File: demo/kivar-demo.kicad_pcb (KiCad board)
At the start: 2 copper layers, 59 x 42 mm, 66 parts, among them U1 24C02, U2 MIC841HYC5, U3 ISL91127IRAZ, U4 TCA9535PWR, U6 AP3032, U7 LDO

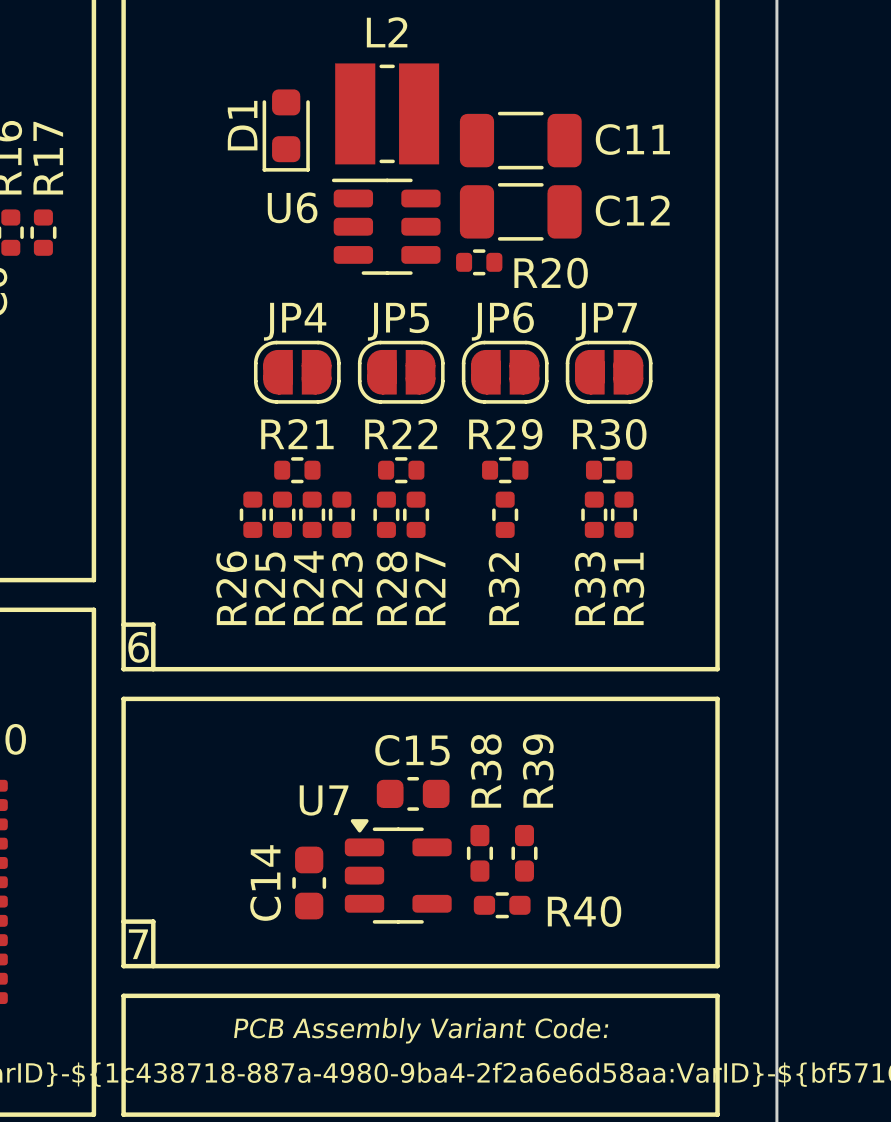
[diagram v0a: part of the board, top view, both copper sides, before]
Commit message: Fix demo project for 0.4.0 re-release
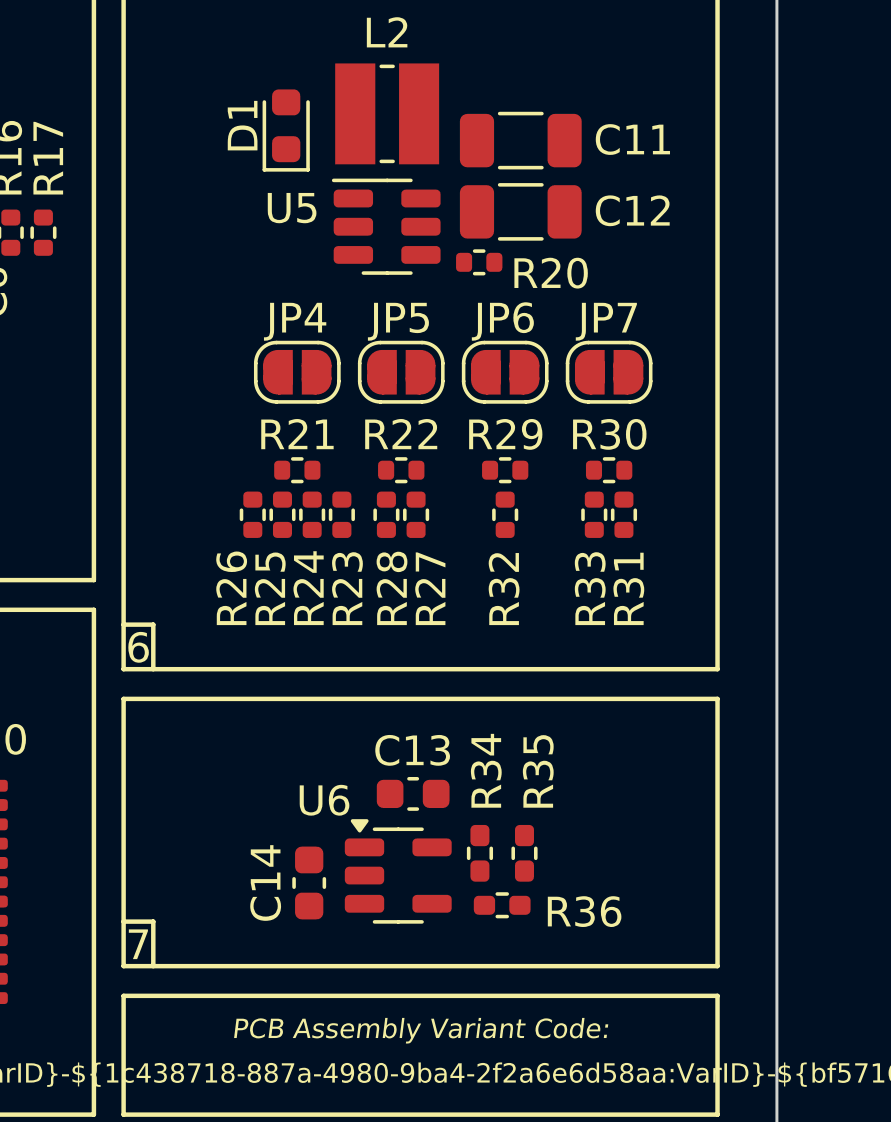
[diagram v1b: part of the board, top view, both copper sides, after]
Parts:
- renumbered C15 to C13, R38 to R34, R39 to R35, R40 to R36, U6 to U5, U7 to U6
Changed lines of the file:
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@@
 	(title_block
 		(title "KiVar Demo Board")
-		(date "2024-09-14")
+		(date "2024-09-16")
 		(rev "0.4.0")
 		(company "Author: Mark Hämmerling <dev@markh.de>")
@@
 	(net 55 "+5V")
 	(net 56 "/Example 7: LDO Output Voltage Selection/VOUT")
-	(net 57 "Net-(U7-FB)")
+	(net 57 "Net-(U6-FB)")
 	(footprint "Resistor_SMD:R_0402_1005Metric"
 		(layer "F.Cu")
@@
 			(at 0 1.17 90)
 			(layer "F.Fab")
+			(hide yes)
 			(effects
 				(font
@@
 			(at 0 1.17 0)
 			(layer "F.Fab")
+			(hide yes)
 			(effects
 				(font
@@
 			(at 0 1.17 90)
 			(layer "F.Fab")
+			(hide yes)
 			(effects
 				(font
@@
 		(descr "SOT, 5 Pin (https://www.jedec.org/sites/default/files/docs/Mo-178c.PDF variant AA), generated with kicad-footprint-generator ipc_gullwing_generator.py")
 		(tags "SOT TO_SOT_SMD")
-		(property "Reference" "U7"
+		(property "Reference" "U6"
 			(at -2.5 -2.5 0)
 			(layer "F.SilkS")
@@
 			(at 0 2.4 0)
 			(layer "F.Fab")
+			(hide yes)
 			(effects
 				(font
@@
 			(layers "F.Cu" "F.Paste" "F.Mask")
 			(roundrect_rratio 0.25)
-			(net 57 "Net-(U7-FB)")
+			(net 57 "Net-(U6-FB)")
 			(pinfunction "FB")
 			(pintype "input")
@@
 			(at 0 1.9 0)
 			(layer "F.Fab")
+			(hide yes)
 			(effects
 				(font
@@
 		(descr "Resistor SMD 0402 (1005 Metric), square (rectangular) end terminal, IPC_7351 nominal with elongated pad for handsoldering. (Body size source: IPC-SM-782 page 72, https://www.pcb-3d.com/wordpress/wp-content/uploads/ipc-sm-782a_amendment_1_and_2.pdf), generated with kicad-footprint-generator")
 		(tags "resistor handsolder")
-		(property "Reference" "R40"
+		(property "Reference" "R36"
 			(at -2.75 -0.25 0)
 			(layer "F.SilkS")
@@
 			(at 0 1.17 0)
 			(layer "F.Fab")
+			(hide yes)
 			(effects
 				(font
@@
 			(layers "F.Cu" "F.Paste" "F.Mask")
 			(roundrect_rratio 0.25)
-			(net 57 "Net-(U7-FB)")
+			(net 57 "Net-(U6-FB)")
 			(pintype "passive")
 		)
@@
 			(at 0 1.43 90)
 			(layer "F.Fab")
+			(hide yes)
 			(effects
 				(font
@@
 			(at 0 1.17 0)
 			(layer "F.Fab")
+			(hide yes)
 			(effects
 				(font
@@
 			(at 0 1.17 90)
 			(layer "F.Fab")
+			(hide yes)
 			(effects
 				(font
@@
 			(at 0 1.85 0)
 			(layer "F.Fab")
+			(hide yes)
 			(effects
 				(font
@@
 			(at 0 1.17 0)
 			(layer "F.Fab")
+			(hide yes)
 			(effects
 				(font
@@
 			(at 0 3.2 0)
 			(layer "F.Fab")
+			(hide yes)
 			(effects
 				(font
@@
 			(at 0 1.9 0)
 			(layer "F.Fab")
+			(hide yes)
 			(effects
 				(font
@@
 		(descr "Capacitor SMD 0603 (1608 Metric), square (rectangular) end terminal, IPC_7351 nominal, (Body size source: IPC-SM-782 page 76, https://www.pcb-3d.com/wordpress/wp-content/uploads/ipc-sm-782a_amendment_1_and_2.pdf), generated with kicad-footprint-generator")
 		(tags "capacitor")
-		(property "Reference" "C15"
+		(property "Reference" "C13"
 			(at 0 -1.43 0)
 			(layer "F.SilkS")
@@
 			(at 0 1.43 0)
 			(layer "F.Fab")
+			(hide yes)
 			(effects
 				(font
@@
 			(at 0 1.17 90)
 			(layer "F.Fab")
+			(hide yes)
 			(effects
 				(font
@@
 		(descr "Resistor SMD 0402 (1005 Metric), square (rectangular) end terminal, IPC_7351 nominal with elongated pad for handsoldering. (Body size source: IPC-SM-782 page 72, https://www.pcb-3d.com/wordpress/wp-content/uploads/ipc-sm-782a_amendment_1_and_2.pdf), generated with kicad-footprint-generator")
 		(tags "resistor handsolder")
-		(property "Reference" "R38"
+		(property "Reference" "R34"
 			(at -2.75 -0.25 90)
 			(layer "F.SilkS")
@@
 			(at 0 1.17 90)
 			(layer "F.Fab")
+			(hide yes)
 			(effects
 				(font
@@
 			)
 		)
-		(property "Var" "1.2V(0Ω) 1.8V(100kΩ) 3.3V(175kΩ)"
+		(property "Var" "1.2V(0Ω) 1.8V(100kΩ) 2.5V(150kΩ) 3.3V(175kΩ)"
 			(at 0 0 -90)
 			(unlocked yes)
@@
 			)
 		)
-		(property "VarID.Var" "1.2V(12) 1.8V(18) 3.3V(33)"
+		(property "VarID.Var" "1.2V(12) 1.8V(18) 2.5V(25) 3.3V(33)"
 			(at 0 0 -90)
 			(unlocked yes)
@@
 			(layers "F.Cu" "F.Paste" "F.Mask")
 			(roundrect_rratio 0.25)
-			(net 57 "Net-(U7-FB)")
+			(net 57 "Net-(U6-FB)")
 			(pintype "passive")
 		)
@@
 			(at 0 1.17 90)
 			(layer "F.Fab")
+			(hide yes)
 			(effects
 				(font
@@
 			(at 0 1.17 0)
 			(layer "F.Fab")
+			(hide yes)
 			(effects
 				(font
@@
 			(at 0 1.85 0)
 			(layer "F.Fab")
+			(hide yes)
 			(effects
 				(font
@@
 			(at 0 1.17 0)
 			(layer "F.Fab")
+			(hide yes)
 			(effects
 				(font
@@
 			(at 0 1.9 0)
 			(layer "F.Fab")
+			(hide yes)
 			(effects
 				(font
@@
 			(at 0 1.17 90)
 			(layer "F.Fab")
+			(hide yes)
 			(effects
 				(font
@@
 			(at 0 1.17 90)
 			(layer "F.Fab")
+			(hide yes)
 			(effects
 				(font
@@
 			(at 0 1.17 90)
 			(layer "F.Fab")
+			(hide yes)
 			(effects
 				(font
@@
 			(at 0 1.17 90)
 			(layer "F.Fab")
+			(hide yes)
 			(effects
 				(font
@@
 			(at 0 1.43 -90)
 			(layer "F.Fab")
+			(hide yes)
 			(effects
 				(font
@@
 			(at 0 1.9 0)
 			(layer "F.Fab")
+			(hide yes)
 			(effects
 				(font
@@
 		(descr "SOT, 6 Pin (https://www.jedec.org/sites/default/files/docs/Mo-178c.PDF variant AB), generated with kicad-footprint-generator ipc_gullwing_generator.py")
 		(tags "SOT TO_SOT_SMD")
-		(property "Reference" "U6"
+		(property "Reference" "U5"
 			(at -3.2 -0.6 0)
 			(layer "F.SilkS")
@@
 			(at 0 2.4 0)
 			(layer "F.Fab")
+			(hide yes)
 			(effects
 				(font
@@
 		(descr "Resistor SMD 0402 (1005 Metric), square (rectangular) end terminal, IPC_7351 nominal with elongated pad for handsoldering. (Body size source: IPC-SM-782 page 72, https://www.pcb-3d.com/wordpress/wp-content/uploads/ipc-sm-782a_amendment_1_and_2.pdf), generated with kicad-footprint-generator")
 		(tags "resistor handsolder")
-		(property "Reference" "R39"
+		(property "Reference" "R35"
 			(at -2.75 -0.5 90)
 			(layer "F.SilkS")
@@
 			(at 0 1.17 90)
 			(layer "F.Fab")
+			(hide yes)
 			(effects
 				(font
@@
 			)
 		)
-		(property "Var" "1.8V(100kΩ) ?(DNP -s!)"
+		(property "Var" "1.8V(100kΩ) 2.5V(390kΩ) ?(DNP -s!)"
 			(at 0 0 -90)
 			(unlocked yes)
@@
 			(layers "F.Cu" "F.Paste" "F.Mask")
 			(roundrect_rratio 0.25)
-			(net 57 "Net-(U7-FB)")
+			(net 57 "Net-(U6-FB)")
 			(pintype "passive")
 		)

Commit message: Update doc info
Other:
- board text added: "https://kivar.markh.de"
- board text removed: "https://github.com/markh-de/KiVar"
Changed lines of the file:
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@@
 	(title_block
 		(title "KiVar Demo Board")
-		(date "2024-09-16")
-		(rev "0.4.0")
+		(date "2025-04-22")
+		(rev "0.5.0")
 		(company "Author: Mark Hämmerling <dev@markh.de>")
-		(comment 3 "https://github.com/markh-de/KiVar")
-		(comment 4 "Download KiVar:")
+		(comment 4 "https://kivar.markh.de")
 	)
 	(layers
@@
 		(layer "Edge.Cuts")
 	)
-	(gr_text "https://github.com/markh-de/KiVar"
+	(gr_text "https://kivar.markh.de"
 		(at 111 112.3 0)
 		(layer "F.SilkS")
